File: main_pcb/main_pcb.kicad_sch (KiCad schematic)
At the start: 54 parts, among them J1 DBG, J2 UI, J3 UI, J4 Raspberry_Pi_Zero_WH, J5 UI, J6 UI, J7 UPDN, J8 ISP, J9 BTN_TRIG, Q1 BSS123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

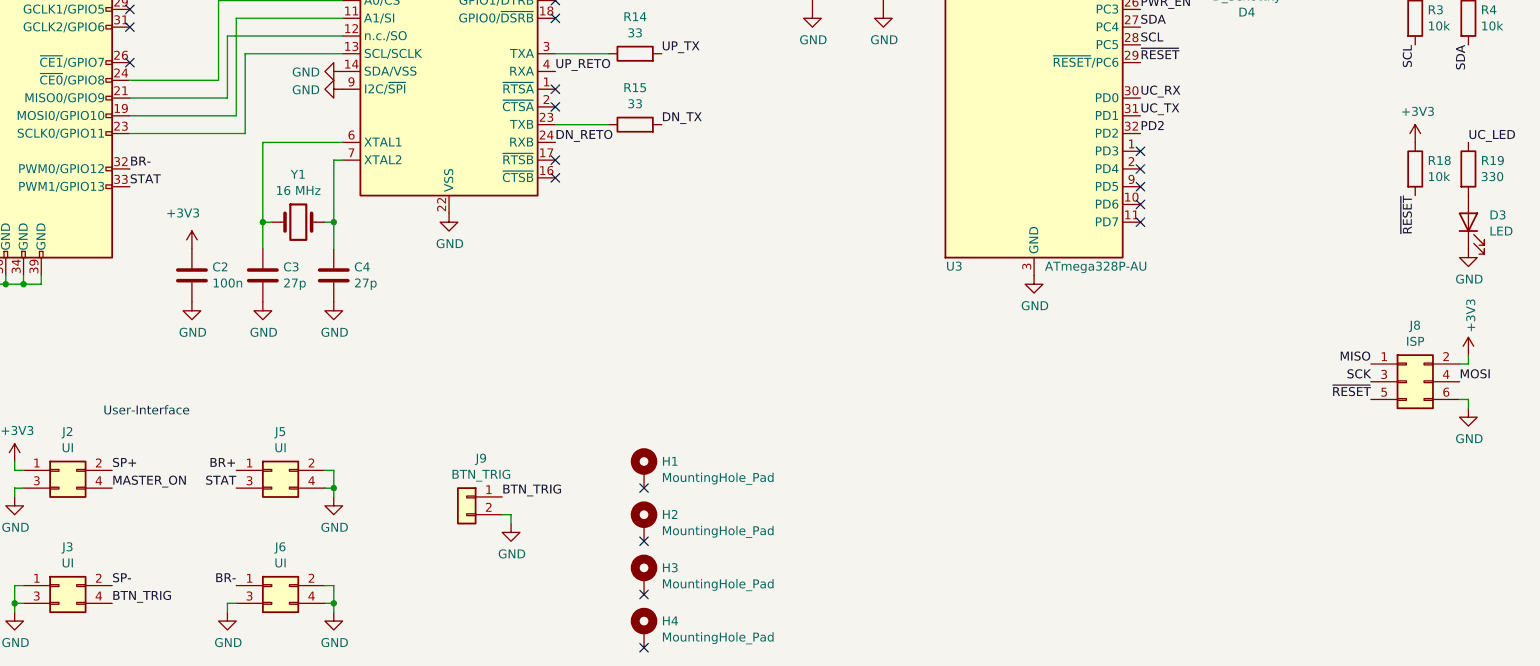
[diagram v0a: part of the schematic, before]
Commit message: Moved the LED control from the Pi to the AVR
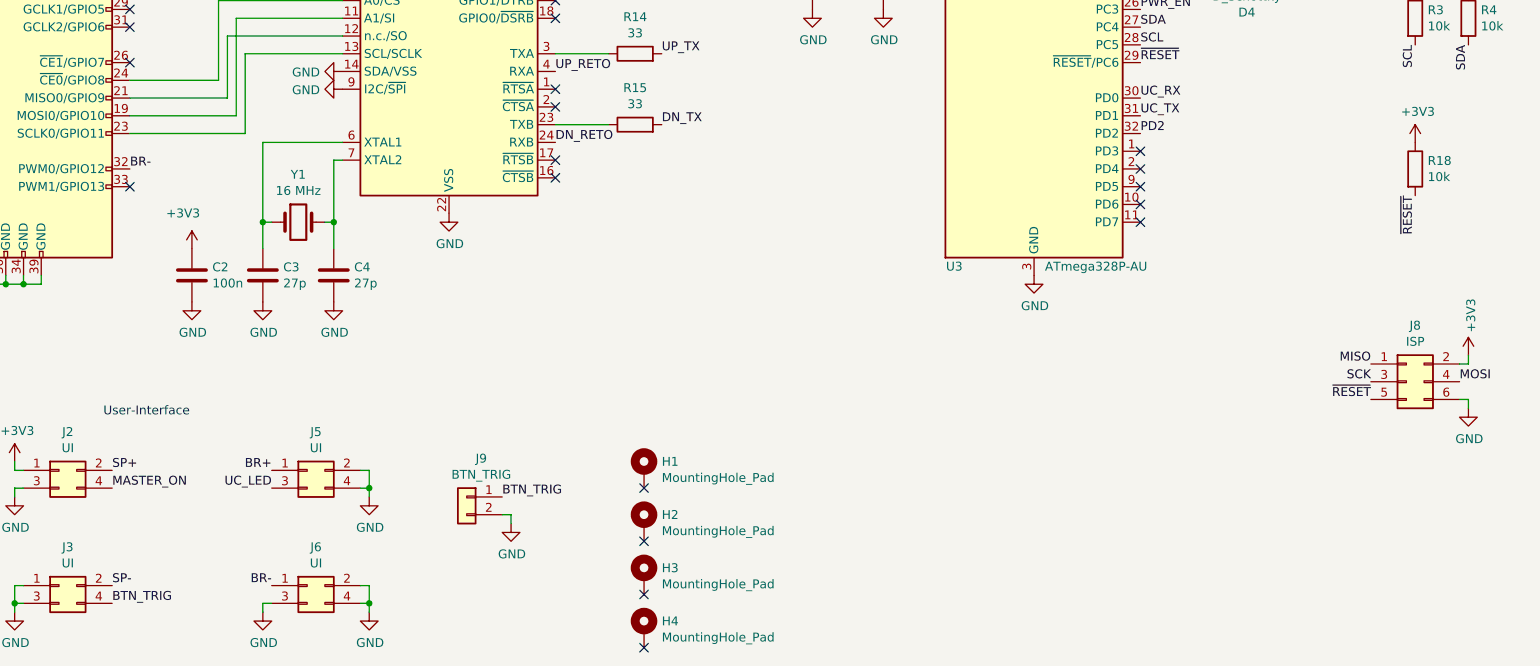
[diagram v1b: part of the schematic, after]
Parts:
- removed D3: LED, LED_SMD:LED_0603_1608Metric, symbol Device:LED
- removed R19: 330, Resistor_SMD:R_0603_1608Metric, symbol Device:R
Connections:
- net UC_LED: now also J5.3 (Pin_3)
- net STAT: no longer names the net of J4.33 (PWM1/GPIO13)
- net STAT: no longer J5.3 (Pin_3)
- no-connect marks 31 -> 32
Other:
- moved on the sheet: J5, J6
